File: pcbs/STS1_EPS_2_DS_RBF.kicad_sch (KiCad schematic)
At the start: 27 parts, among them Q1 2N7002, Q10 2N7002, Q11 2N7002, Q14 2N7002, Q15 2N7002, Q18 2N7002, Q19 2N7002, Q20 2N7002, Q7 2N7002

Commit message: Signals to the bus gate should now be provided with supply voltage the proper way.
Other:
- note added: "Open drain outputs"
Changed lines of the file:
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@@
+		)
+	)
+	(text "Open drain outputs"
+		(exclude_from_sim no)
+		(at 210.566 21.082 0)
+		(effects
+			(font
+				(size 1.27 1.27)
+			)
+		)
+	)
+	(text "Open drain outputs"
+		(exclude_from_sim no)
+		(at 90.17 19.812 0)
+		(effects
+			(font
+				(size 1.27 1.27)
+			)
+		)
+	)
+	(text "Open drain outputs"
+		(exclude_from_sim no)
+		(at 83.312 63.754 0)
+		(effects
+			(font
+				(size 1.27 1.27)
+			)
 		)
 	)

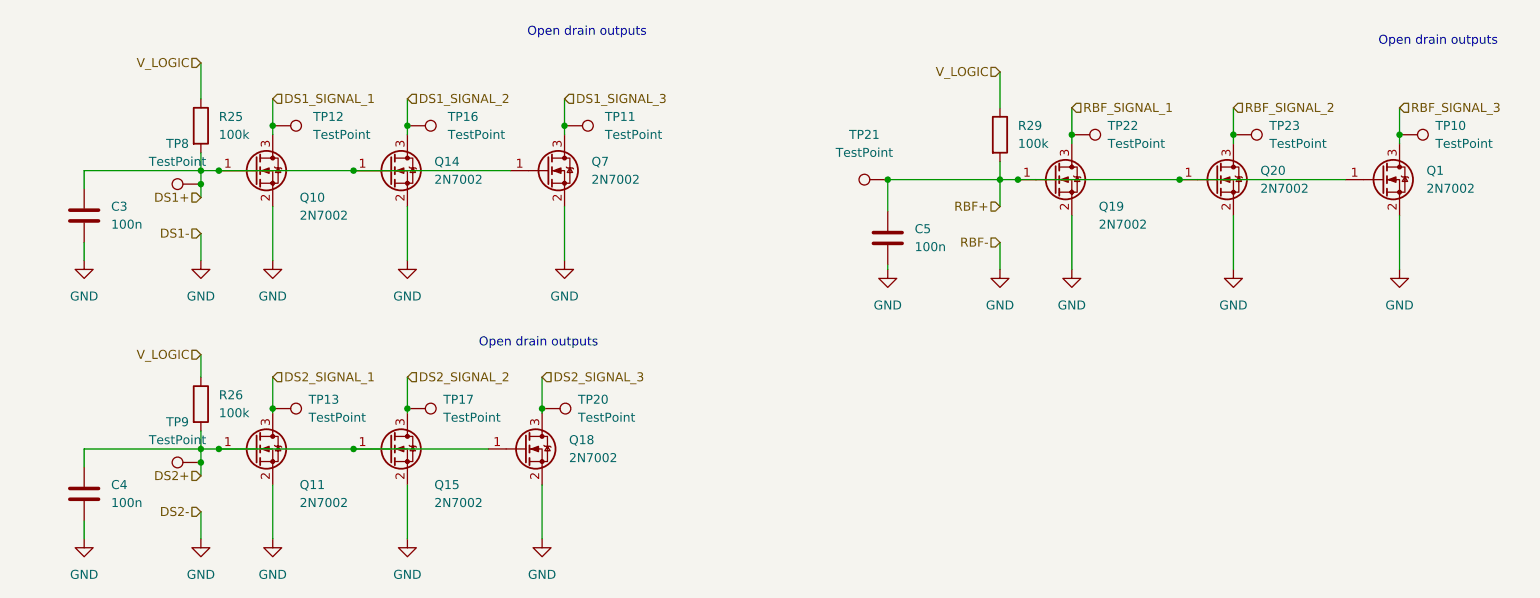
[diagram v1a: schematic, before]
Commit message: Added possibilities to short single interrupt sources.
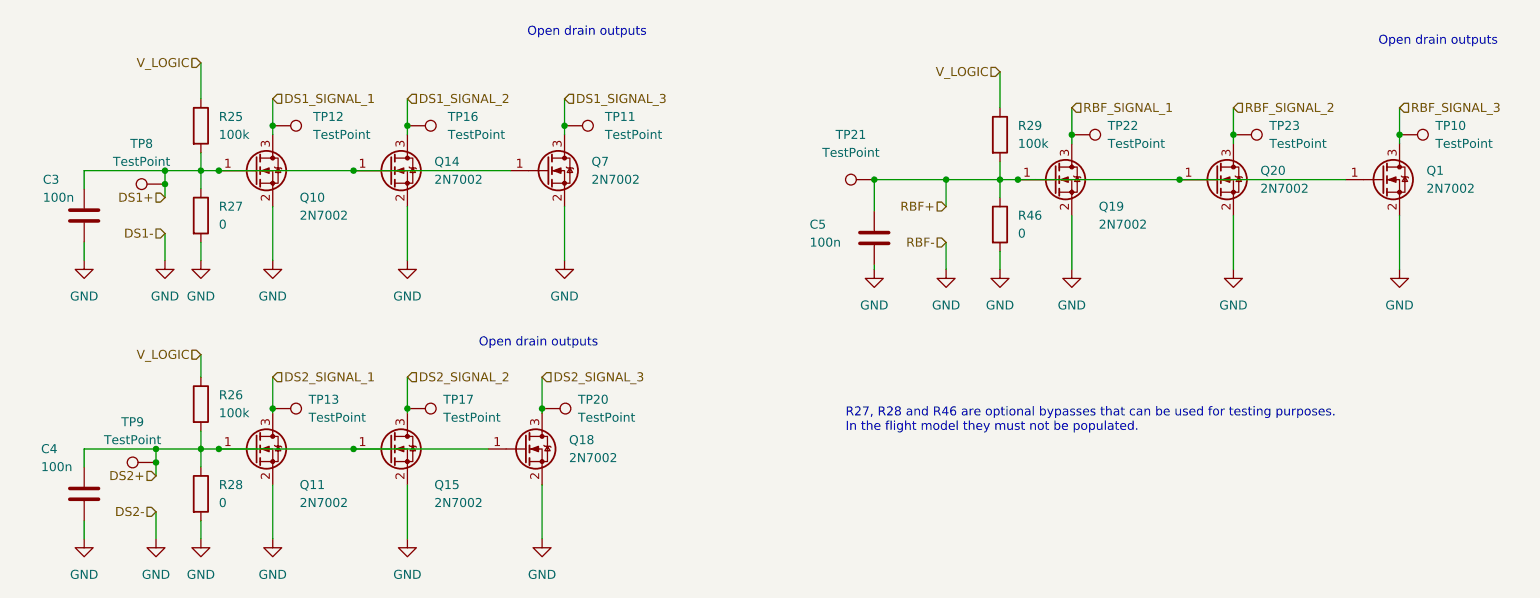
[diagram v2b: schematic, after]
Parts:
- added R27, R28, R46: 0, Resistor_SMD:R_0805_2012Metric, symbol Device:R
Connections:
- net DS1+: now also R27.1
- net DS2+: now also R28.1
- net GND: now also R27.2, R28.2, R46.2
- net RBF+: now also R46.1
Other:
- note added: "R27, R28 and R46 are optional bypasses that can be used for testing purposes. In the flight model they must not be populated."
- moved on the sheet: C5, TP21, TP8, TP9

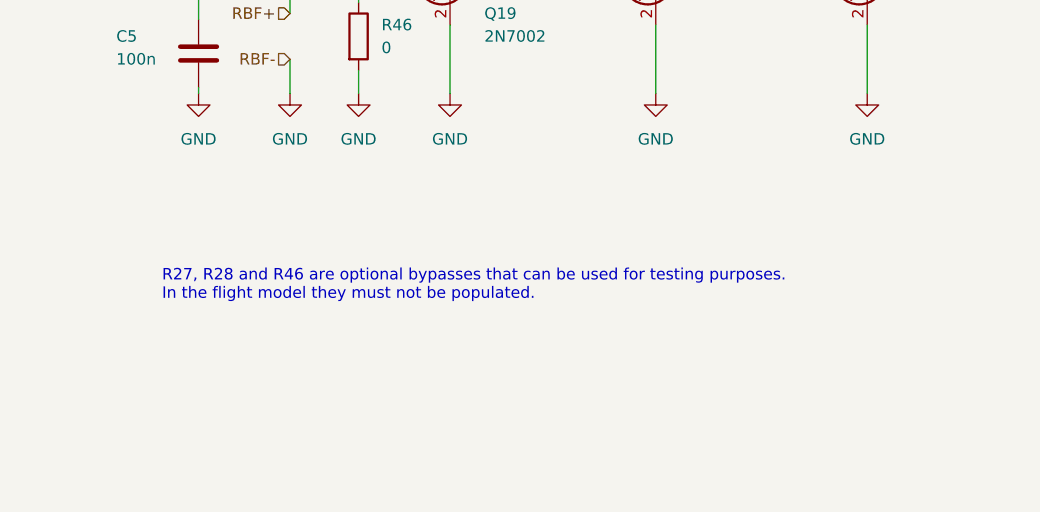
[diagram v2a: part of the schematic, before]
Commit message: Fixed the logic behing the GATE_SIGNAL signal.
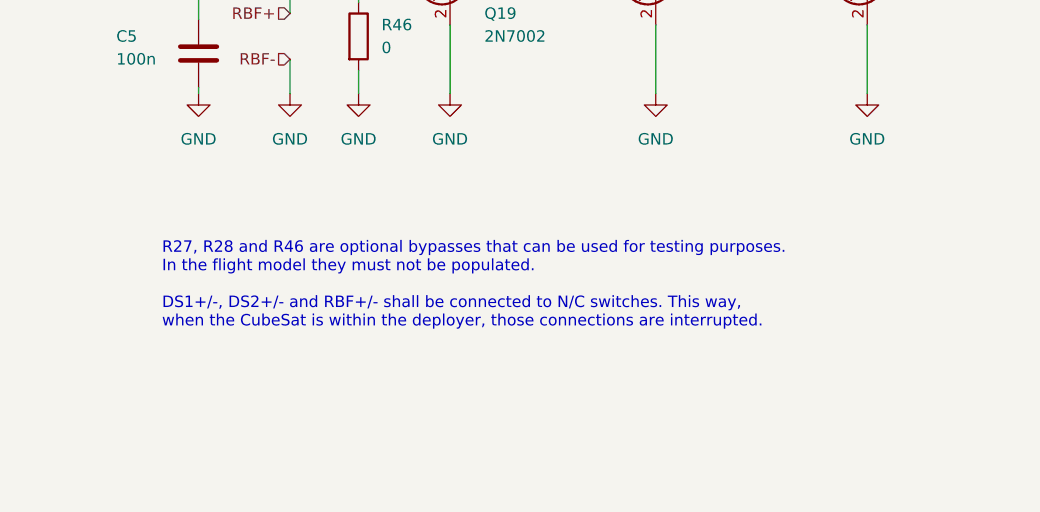
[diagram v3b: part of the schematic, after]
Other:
- note added: "R27, R28 and R46 are optional bypasses that can be used for testing purposes. In the flight model they must not be populated. DS1+/-, DS2+/- and RBF+/- shall be connected to N/C switches. This way, when the CubeSat is within the deployer, those connections are interrupted."
- note removed: "R27, R28 and R46 are optional bypasses that can be used for testing purposes. In the flight model they must not be populated."
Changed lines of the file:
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@@
 		)
 	)
-	(text "R27, R28 and R46 are optional bypasses that can be used for testing purposes.\nIn the flight model they must not be populated."
+	(text "R27, R28 and R46 are optional bypasses that can be used for testing purposes.\nIn the flight model they must not be populated.\n\nDS1+/-, DS2+/- and RBF+/- shall be connected to N/C switches. This way, \nwhen the CubeSat is within the deployer, those connections are interrupted."
 		(exclude_from_sim no)
 		(at 126.746 74.676 0)

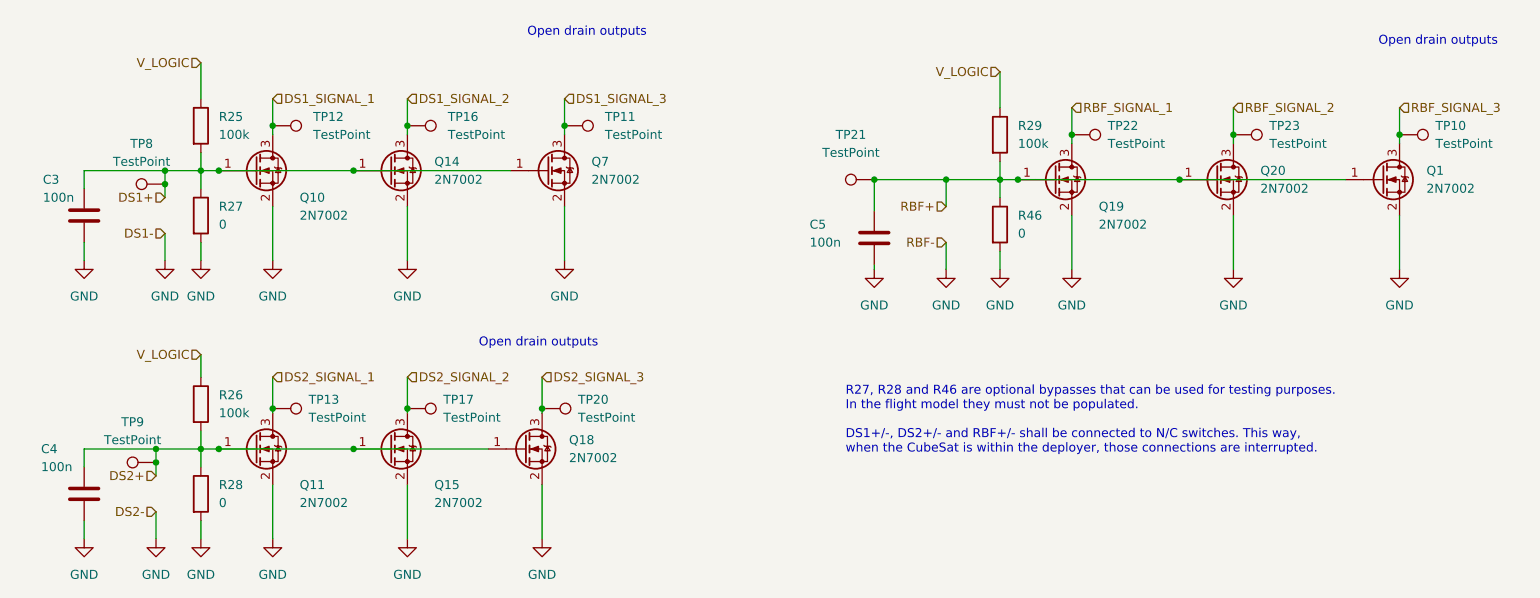
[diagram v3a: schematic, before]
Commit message: Added even more ESD protection.
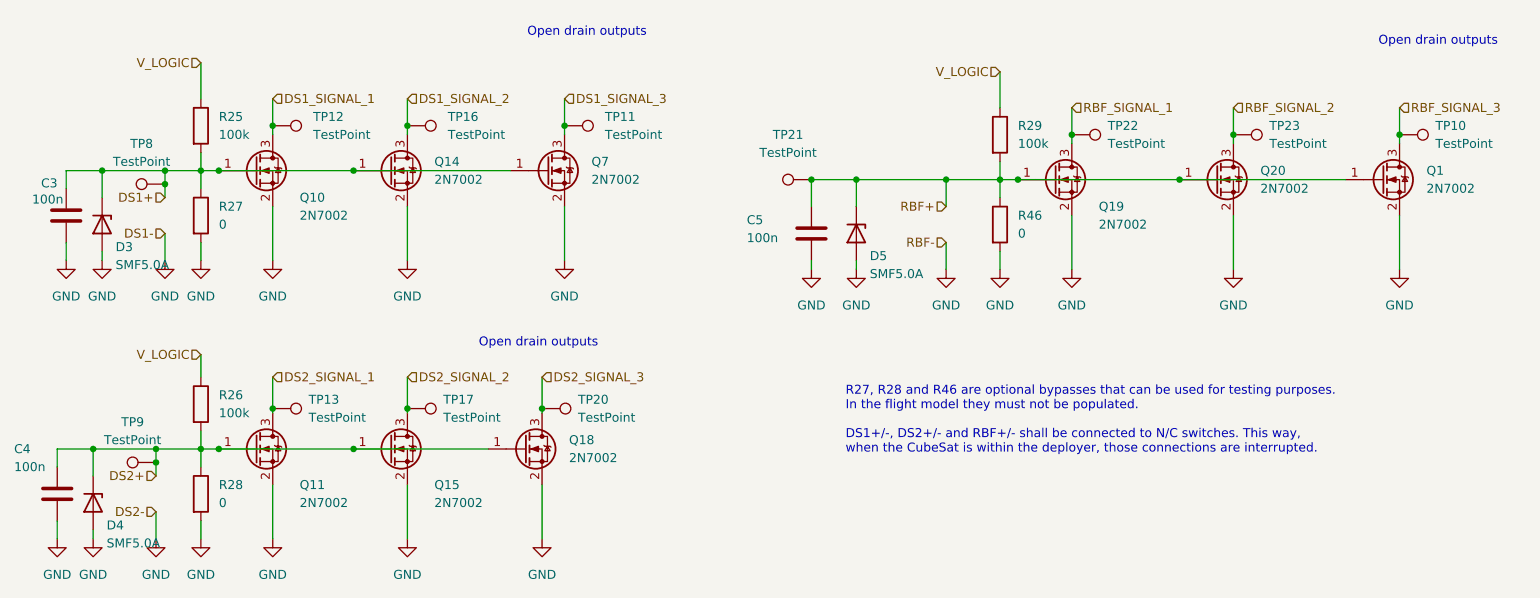
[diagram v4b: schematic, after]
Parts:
- added D3, D4, D5: SMF5.0A, Diode_SMD:D_SMF, symbol Device:D_Zener
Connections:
- net DS1+: now also D3.1 (K)
- net DS2+: now also D4.1 (K)
- net GND: now also D3.2 (A), D4.2 (A), D5.2 (A)
- net RBF+: now also D5.1 (K)
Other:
- moved on the sheet: C3, C4, C5, TP21

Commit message: Fixed some warnings and errors.
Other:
- moved on the sheet: Q1, Q7, TP10, TP11, TP13, TP17, TP20, TP8, TP9

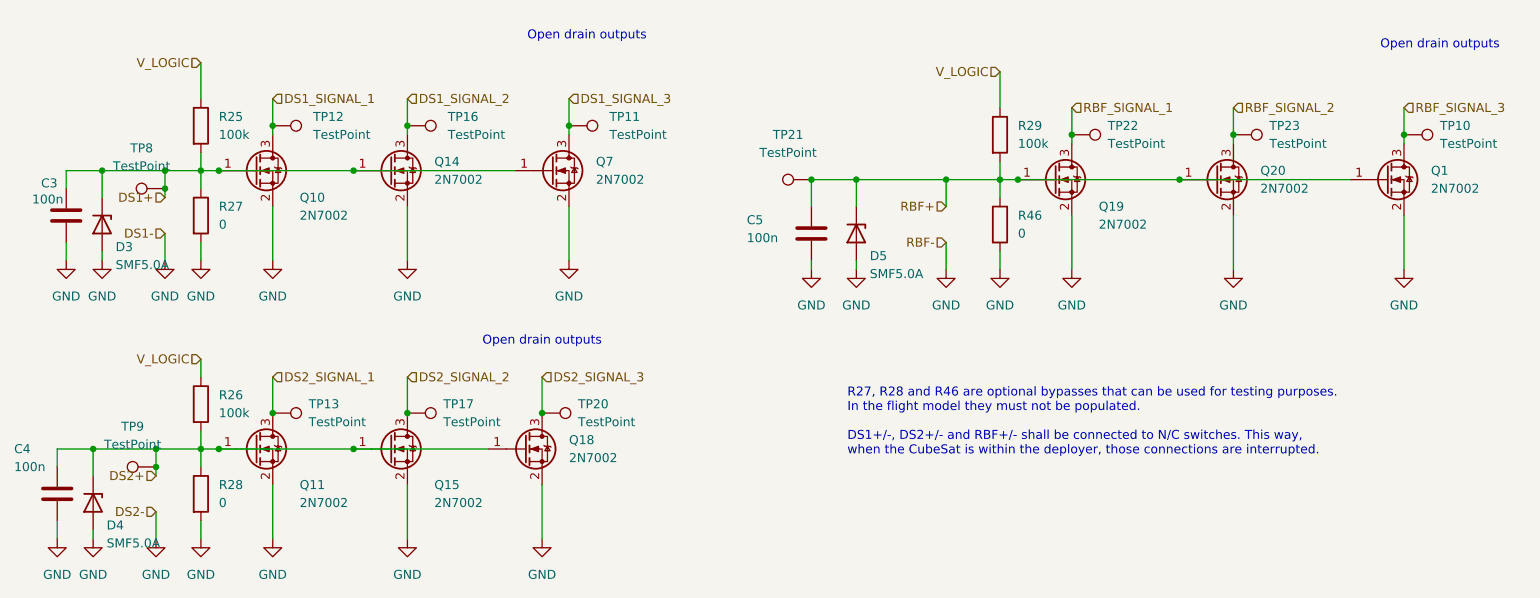
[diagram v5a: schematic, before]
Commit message: Marked optional bypasses as "Do not place".
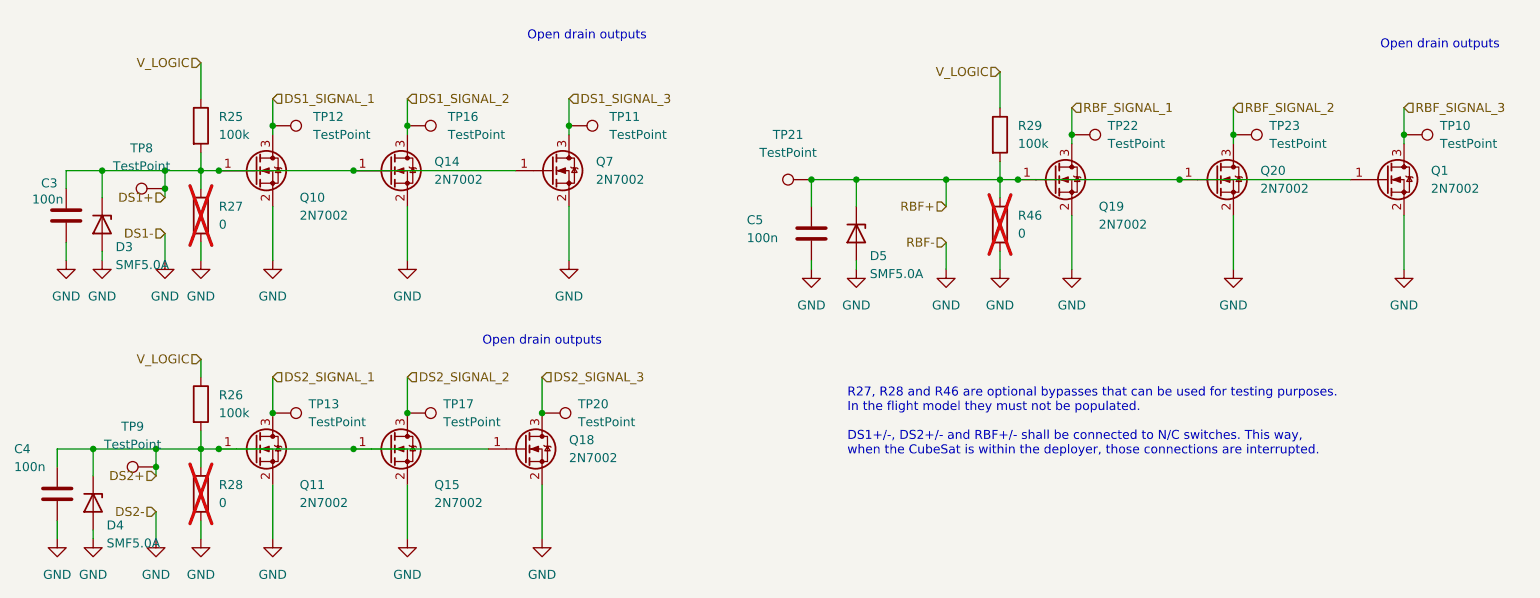
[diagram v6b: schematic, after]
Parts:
- R27, R28, R46: now not fitted
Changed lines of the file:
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@@
 		(in_bom yes)
 		(on_board yes)
-		(dnp no)
+		(dnp yes)
 		(fields_autoplaced yes)
 		(property "Reference" "R46"
@@
 		(in_bom yes)
 		(on_board yes)
-		(dnp no)
+		(dnp yes)
 		(fields_autoplaced yes)
 		(property "Reference" "R27"
@@
 		(in_bom yes)
 		(on_board yes)
-		(dnp no)
+		(dnp yes)
 		(fields_autoplaced yes)
 		(property "Reference" "R28"

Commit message: Added more part numbers.
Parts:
- C3, C4, C5: Part Nr. (none) -> C0805T104K1RCLTU
- R25, R26, R29: Part Nr. (none) -> TNPW0805100KFEEA
